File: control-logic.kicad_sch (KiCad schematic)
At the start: 0 parts

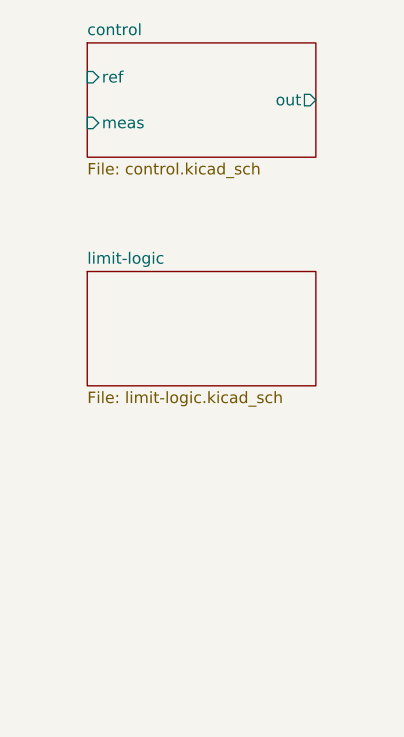
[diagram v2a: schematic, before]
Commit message: add limit-logic hierarchical labels
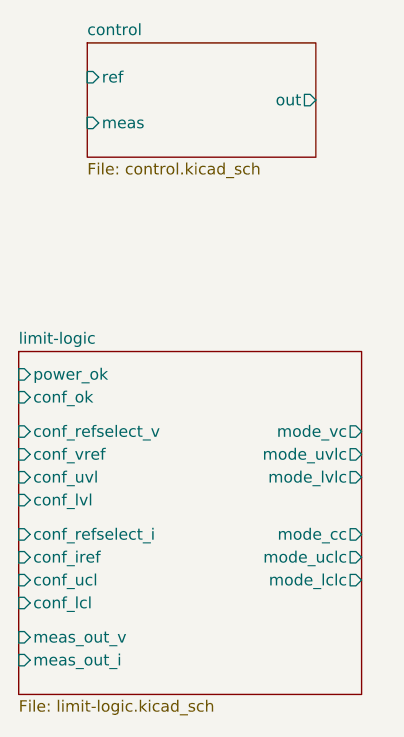
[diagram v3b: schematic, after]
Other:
- sheet limit-logic ports: added conf_iref, conf_lcl, conf_lvl, conf_ok, conf_refselect_i, conf_refselect_v, conf_ucl, conf_uvl, conf_vref, meas_out_i, meas_out_v, mode_cc, mode_lclc, mode_lvlc, mode_uclc, mode_uvlc, mode_vc, power_ok; removed none
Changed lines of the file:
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@@
 	)
 	(sheet
-		(at 134.62 105.41)
-		(size 25.4 12.7)
+		(at 127 114.3)
+		(size 38.1 38.1)
 		(fields_autoplaced yes)
 		(stroke
@@
 		)
 		(property "Sheetname" "limit-logic"
-			(at 134.62 104.6984 0)
+			(at 127 113.5884 0)
 			(effects
 				(font
@@
 		)
 		(property "Sheetfile" "limit-logic.kicad_sch"
-			(at 134.62 118.6946 0)
+			(at 127 152.9846 0)
 			(effects
 				(font
@@
 			)
 		)
+		(pin "meas_out_i" input
+			(at 127 148.59 180)
+			(effects
+				(font
+					(size 1.27 1.27)
+				)
+				(justify left)
+			)
+		)
+		(pin "conf_lvl" input
+			(at 127 130.81 180)
+			(effects
+				(font
+					(size 1.27 1.27)
+				)
+				(justify left)
+			)
+		)
+		(pin "meas_out_v" input
+			(at 127 146.05 180)
+			(effects
+				(font
+					(size 1.27 1.27)
+				)
+				(justify left)
+			)
+		)
+		(pin "conf_uvl" input
+			(at 127 128.27 180)
+			(effects
+				(font
+					(size 1.27 1.27)
+				)
+				(justify left)
+			)
+		)
+		(pin "power_ok" input
+			(at 127 116.84 180)
+			(effects
+				(font
+					(size 1.27 1.27)
+				)
+				(justify left)
+			)
+		)
+		(pin "conf_ok" input
+			(at 127 119.38 180)
+			(effects
+				(font
+					(size 1.27 1.27)
+				)
+				(justify left)
+			)
+		)
+		(pin "conf_vref" input
+			(at 127 125.73 180)
+			(effects
+				(font
+					(size 1.27 1.27)
+				)
+				(justify left)
+			)
+		)
+		(pin "conf_iref" input
+			(at 127 137.16 180)
+			(effects
+				(font
+					(size 1.27 1.27)
+				)
+				(justify left)
+			)
+		)
+		(pin "conf_lcl" input
+			(at 127 142.24 180)
+			(effects
+				(font
+					(size 1.27 1.27)
+				)
+				(justify left)
+			)
+		)
+		(pin "conf_ucl" input
+			(at 127 139.7 180)
+			(effects
+				(font
+					(size 1.27 1.27)
+				)
+				(justify left)
+			)
+		)
+		(pin "conf_refselect_v" input
+			(at 127 123.19 180)
+			(effects
+				(font
+					(size 1.27 1.27)
+				)
+				(justify left)
+			)
+		)
+		(pin "conf_refselect_i" input
+			(at 127 134.62 180)
+			(effects
+				(font
+					(size 1.27 1.27)
+				)
+				(justify left)
+			)
+		)
+		(pin "mode_lclc" output
+			(at 165.1 139.7 0)
+			(effects
+				(font
+					(size 1.27 1.27)
+				)
+				(justify right)
+			)
+		)
+		(pin "mode_vc" output
+			(at 165.1 123.19 0)
+			(effects
+				(font
+					(size 1.27 1.27)
+				)
+				(justify right)
+			)
+		)
+		(pin "mode_uclc" output
+			(at 165.1 137.16 0)
+			(effects
+				(font
+					(size 1.27 1.27)
+				)
+				(justify right)
+			)
+		)
+		(pin "mode_uvlc" output
+			(at 165.1 125.73 0)
+			(effects
+				(font
+					(size 1.27 1.27)
+				)
+				(justify right)
+			)
+		)
+		(pin "mode_lvlc" output
+			(at 165.1 128.27 0)
+			(effects
+				(font
+					(size 1.27 1.27)
+				)
+				(justify right)
+			)
+		)
+		(pin "mode_cc" output
+			(at 165.1 134.62 0)
+			(effects
+				(font
+					(size 1.27 1.27)
+				)
+				(justify right)
+			)
+		)
